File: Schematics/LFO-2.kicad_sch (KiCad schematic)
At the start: 81 parts, among them J16 Conn_01x03, J17 Conn_01x10h, J18 Conn_01x05, J19 Conn_01x03, J89 Conn_01x03, Q12 BSS138, Q13 BSS138, U41 LM324, U42 LM324, U43 ADG419BN, U44 LM78L05, U45 SSI2130, U93 PCF8574, U94 AMS1117-3.3

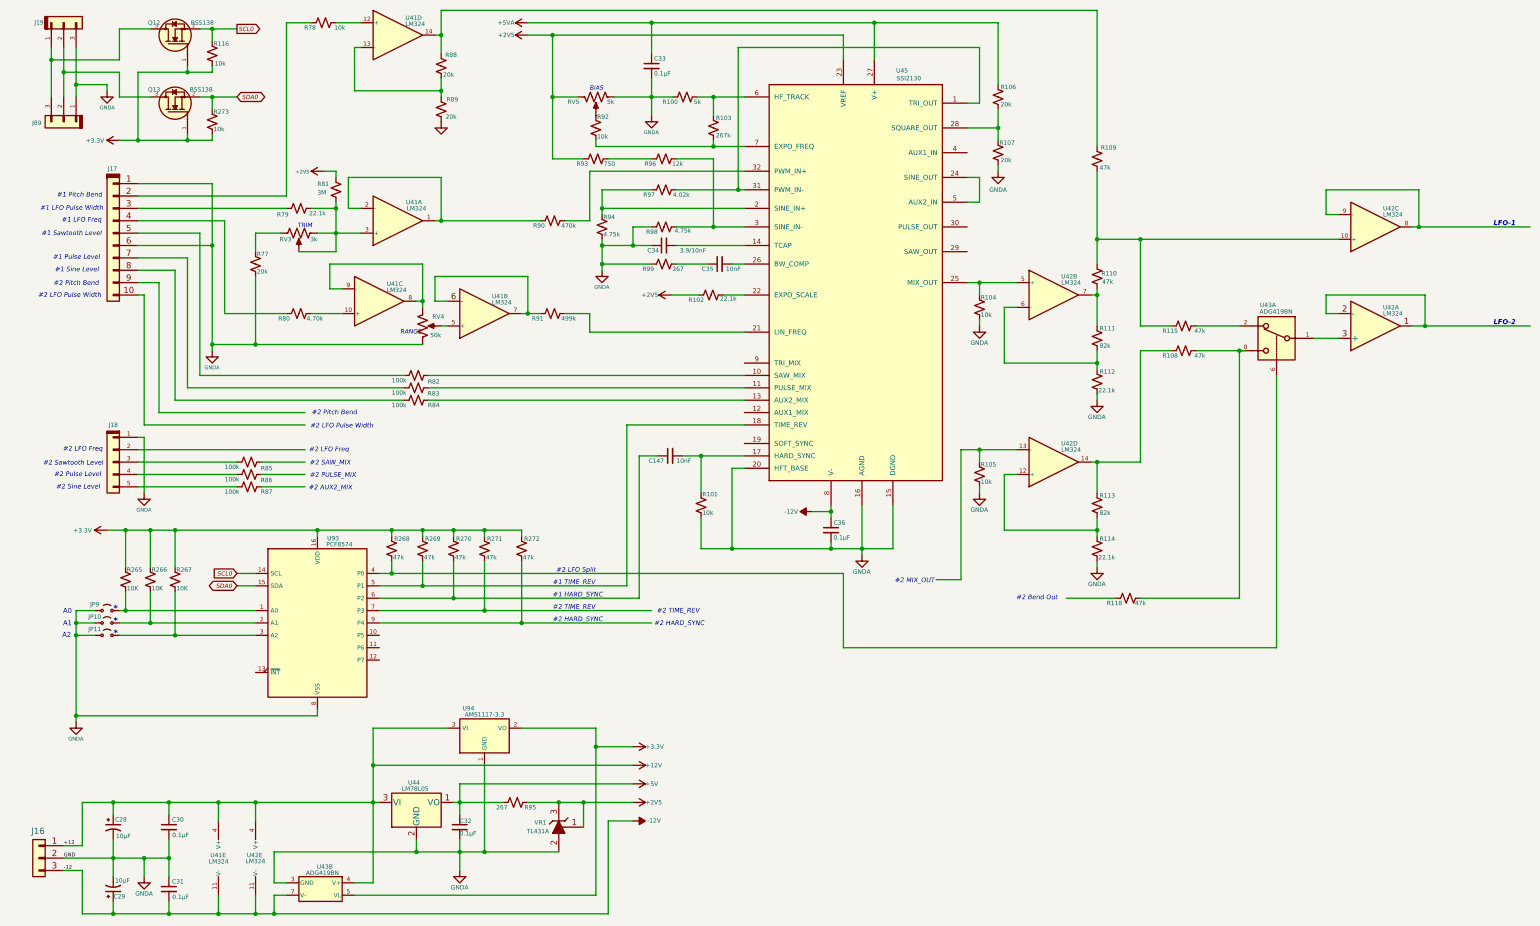
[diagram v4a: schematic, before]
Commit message: Cleaned up page advance on display controls.
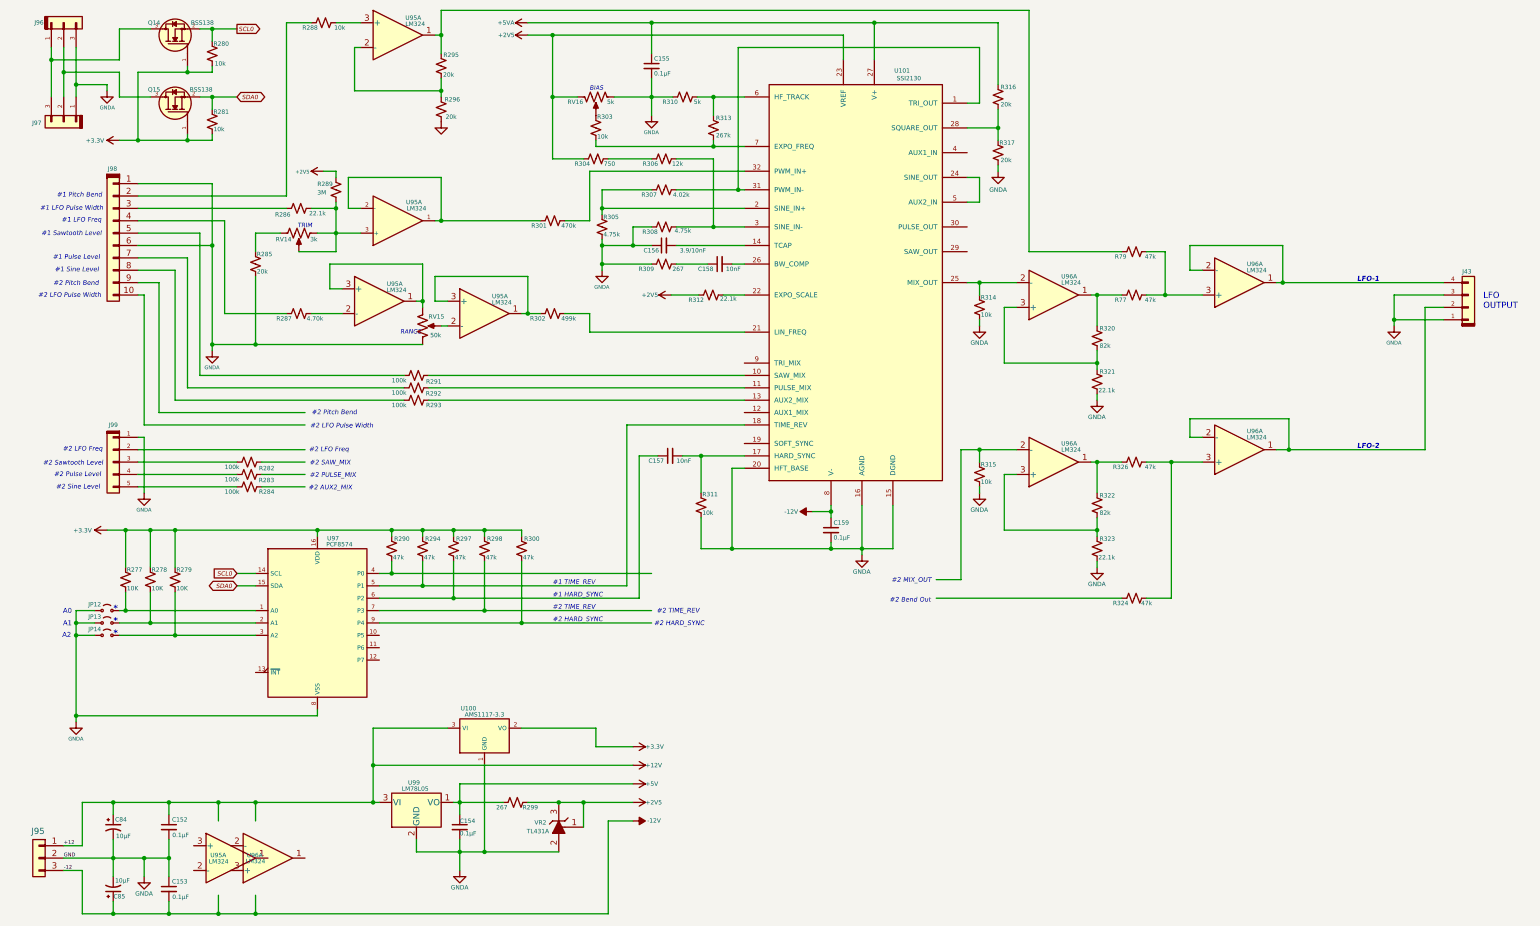
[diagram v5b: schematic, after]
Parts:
- removed R109, R110, R115: 47k, symbol Device:R_Small_US
- removed U43: ADG419BN, Package_DIP:DIP-8_W7.62mm, symbol Analog_Switch:ADG419BN
- added J43: Conn_01x04, symbol My Connectors:Conn_01x04
- added R77, R79: 47k, symbol Device:R_Small_US
- renumbered C30 to C152, C31 to C153, C32 to C154, C33 to C155, C34 to C156, C147 to C157, C35 to C158, C36 to C159, C28 to C84, C29 to C85, J16 to J95, J19 to J96, J89 to J97, J17 to J98, J18 to J99, JP9 to JP12, JP10 to JP13, JP11 to JP14, Q12 to Q14, Q13 to Q15, R265 to R277, R266 to R278, R267 to R279, R116 to R280, R273 to R281, R85 to R282, R86 to R283, R87 to R284, R77 to R285, R79 to R286, R80 to R287, R78 to R288, R81 to R289, R268 to R290, R82 to R291, R83 to R292, R84 to R293, R269 to R294, R88 to R295, R89 to R296, R270 to R297, R271 to R298, R95 to R299, R272 to R300, R90 to R301, R91 to R302, R92 to R303, R93 to R304, R94 to R305, R96 to R306, R97 to R307, R98 to R308, R99 to R309, R100 to R310, R101 to R311, R102 to R312, R103 to R313, R104 to R314, R105 to R315, R106 to R316, R107 to R317, R111 to R320, R112 to R321, R113 to R322, R114 to R323, R118 to R324, R108 to R326, RV3 to RV14, RV4 to RV15, RV5 to RV16, U94 to U100, U45 to U101, U41 to U95, U42 to U96, U93 to U97, U44 to U99, VR1 to VR2
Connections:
- net +12V: no longer U95.4 (V+), U96.4 (V+)
- net -12V: no longer U95.11 (V-), U96.11 (V-)
- net GNDA: now also J43.1 (Pin_1), J43.3 (Pin_3)
- net at R322.2, R323.1: now also U96.3 (+); no longer U96.12 (+)
- net at R315.1: now also U96.2 (-); no longer U96.13 (-)
- net at R322.1, R326.1: now also U96.1; no longer U96.14
- net at R324.2, R326.2: now also U96.3 (+)
- net at R314.1, U101.25 (MIX_OUT): now also U96.2 (-); no longer U96.5 (+)
- net at R320.2, R321.1: now also U96.3 (+); no longer U96.6 (-)
- net at R320.1: now also U96.1, R77.1; no longer U96.7
- net at R288.2: now also U95.3 (+); no longer U95.12 (+)
- net at R295.1, R296.1: now also U95.2 (-); no longer U95.13 (-)
- net at R295.2: now also U95.1, R79.1; no longer U95.14
- net at R287.2: now also U95.2 (-); no longer U95.10 (+)
- net at U96.1, U96.2 (-): now also J43.2 (Pin_2)
- new net: R302.1, U95.1, U95.3 (+)
- new net: RV15. (2), U95.2 (-)
- new net: RV15. (2), U95.1, U95.3 (+)
- new net: J43.4 (Pin_4), U96.1, U96.2 (-)
- new net: R77.2, R79.2, U96.3 (+)
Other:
- note added: "LFO OUTPUT"
- note removed: "#2 LFO Split"
- moved on the sheet: R324, R326, U96A

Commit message: minor adjustments for modulation control interface.
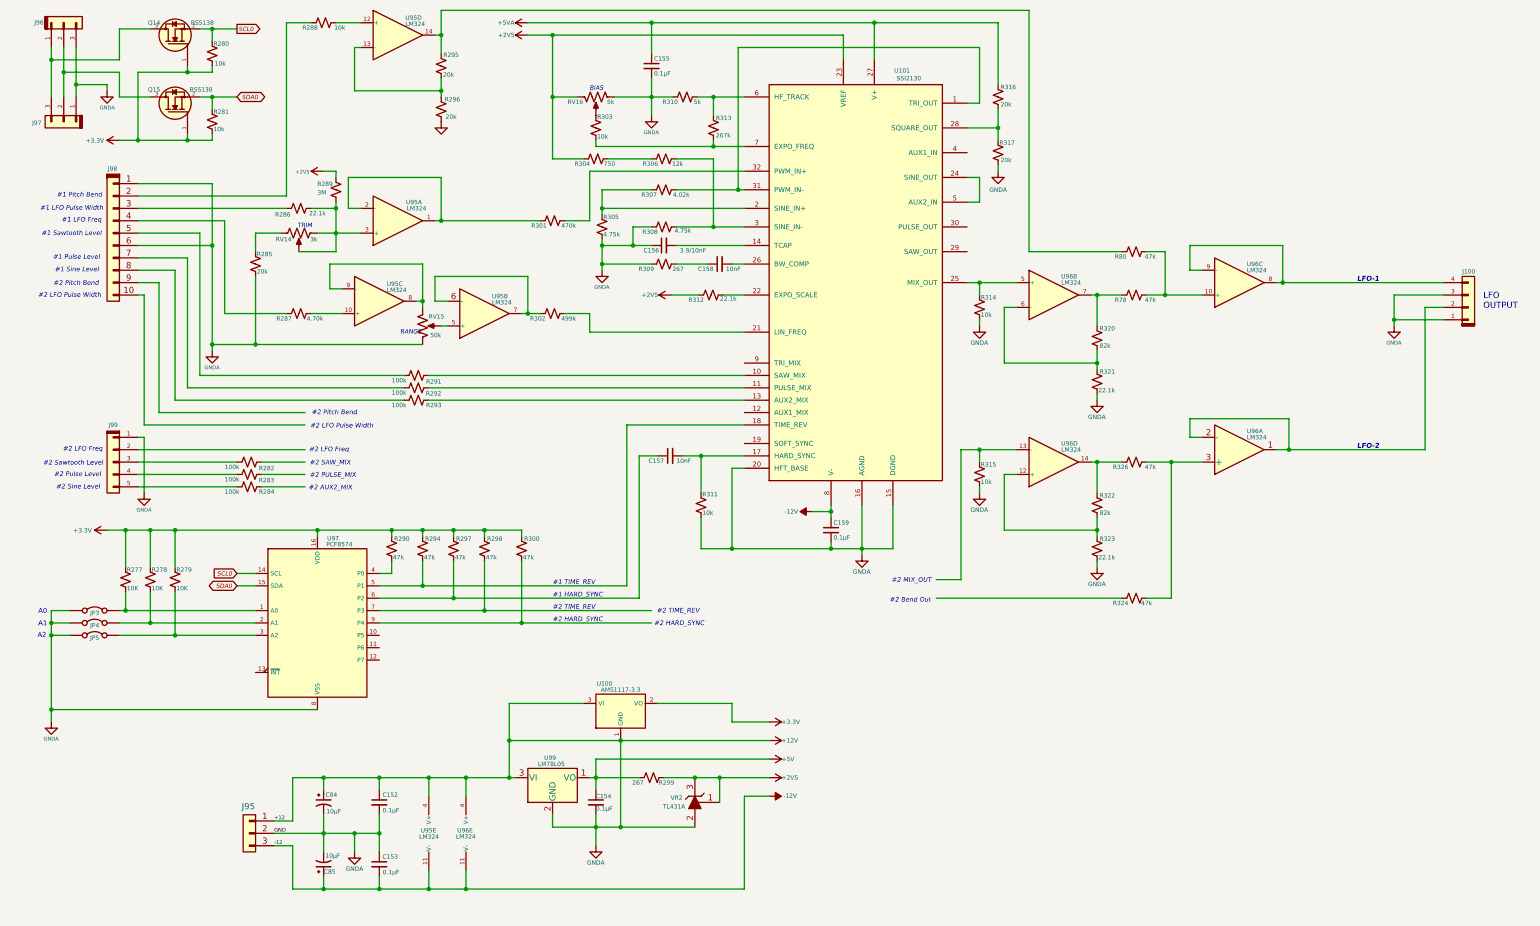
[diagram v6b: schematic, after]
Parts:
- removed JP12, JP13, JP14: Jumper_2_Small_Open, symbol Jumper:Jumper_2_Small_Open
- added JP3, JP4, JP5: Jumper_2_Bridged, symbol Jumper:Jumper_2_Bridged
- renumbered J43 to J100, R77 to R78, R79 to R80
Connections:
- net +12V: now also C152.2, C153.1, C154.2, C155.2, C156.1, C159.2, C84.2, C85.2, J100.1 (Pin_1), J100.3 (Pin_3), J95.2 (Pin_2), J96.3 (Pin_3), J97.1 (Pin_1), J98.1 (Pin_1), J98.6 (Pin_6), J99.1 (Pin_1), R285.2, R296.2, R305.2, R308.1, R309.1, R310.1, R311.2, R314.2, R315.2, R317.2, R321.2, R323.2, RV15. (2), RV16. (2), U100.1 (GND), U101.15 (DGND), U101.16 (AGND), U101.20 (HFT_BASE), U95.4 (V+), U96.4 (V+), U97.8 (VSS), U99.2 (GND), VR2.2 (A), JP3.1 (A), JP4.1 (A), JP5.1 (A)
- net -12V: now also U95.11 (V-), U96.11 (V-)
- net at R322.1, R326.1: now also U96.14; no longer U96.1
- net at R315.1: now also U96.13 (-); no longer U96.2 (-)
- net at R322.2, R323.1: now also U96.12 (+); no longer U96.3 (+)
- net at R320.1, R78.1: now also U96.7; no longer U96.1
- net at R314.1, U101.25 (MIX_OUT): now also U96.5 (+); no longer U96.2 (-)
- net at R320.2, R321.1: now also U96.6 (-); no longer U96.3 (+)
- net at R295.2, R80.1: now also U95.14; no longer U95.1
- net at R295.1, R296.1: now also U95.13 (-); no longer U95.2 (-)
- net at R288.2: now also U95.12 (+); no longer U95.3 (+)
- net at R287.2: now also U95.10 (+); no longer U95.2 (-)
- net at R278.2, U97.2 (A1): now also JP4.2 (B)
- net at R78.2, R80.2: now also U96.10 (+); no longer U96.3 (+)
- net at R279.2, U97.3 (A2): now also JP5.2 (B)
- net at R277.2, U97.1 (A0): now also JP3.2 (B)
- removed net GNDA: C152.2, C153.1, C154.2, C155.2, C156.1, C159.2, C84.2, C85.2, J100.1 (Pin_1), J100.3 (Pin_3), J95.2 (Pin_2), J96.3 (Pin_3), J97.1 (Pin_1), J98.1 (Pin_1), J98.6 (Pin_6), J99.1 (Pin_1), R285.2, R296.2, R305.2, R308.1, R309.1, R310.1, R311.2, R314.2, R315.2, R317.2, R321.2, R323.2, RV15. (2), RV16. (2), U100.1 (GND), U101.15 (DGND), U101.16 (AGND), U101.20 (HFT_BASE), U97.8 (VSS), U99.2 (GND), VR2.2 (A)
- new net: RV15. (2), U95.5 (+)
- new net: R302.1, U95.6 (-), U95.7
- new net: RV15. (2), U95.8, U95.9 (-)
- new net: J100.4 (Pin_4), U96.8, U96.9 (-)
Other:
- note removed: "*"
- moved on the sheet: C152, C153, C154, C84, C85, J95, R299, U100, U99, VR2

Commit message: Added support hardware for LFO output matrix and calibration analog to digital converter.
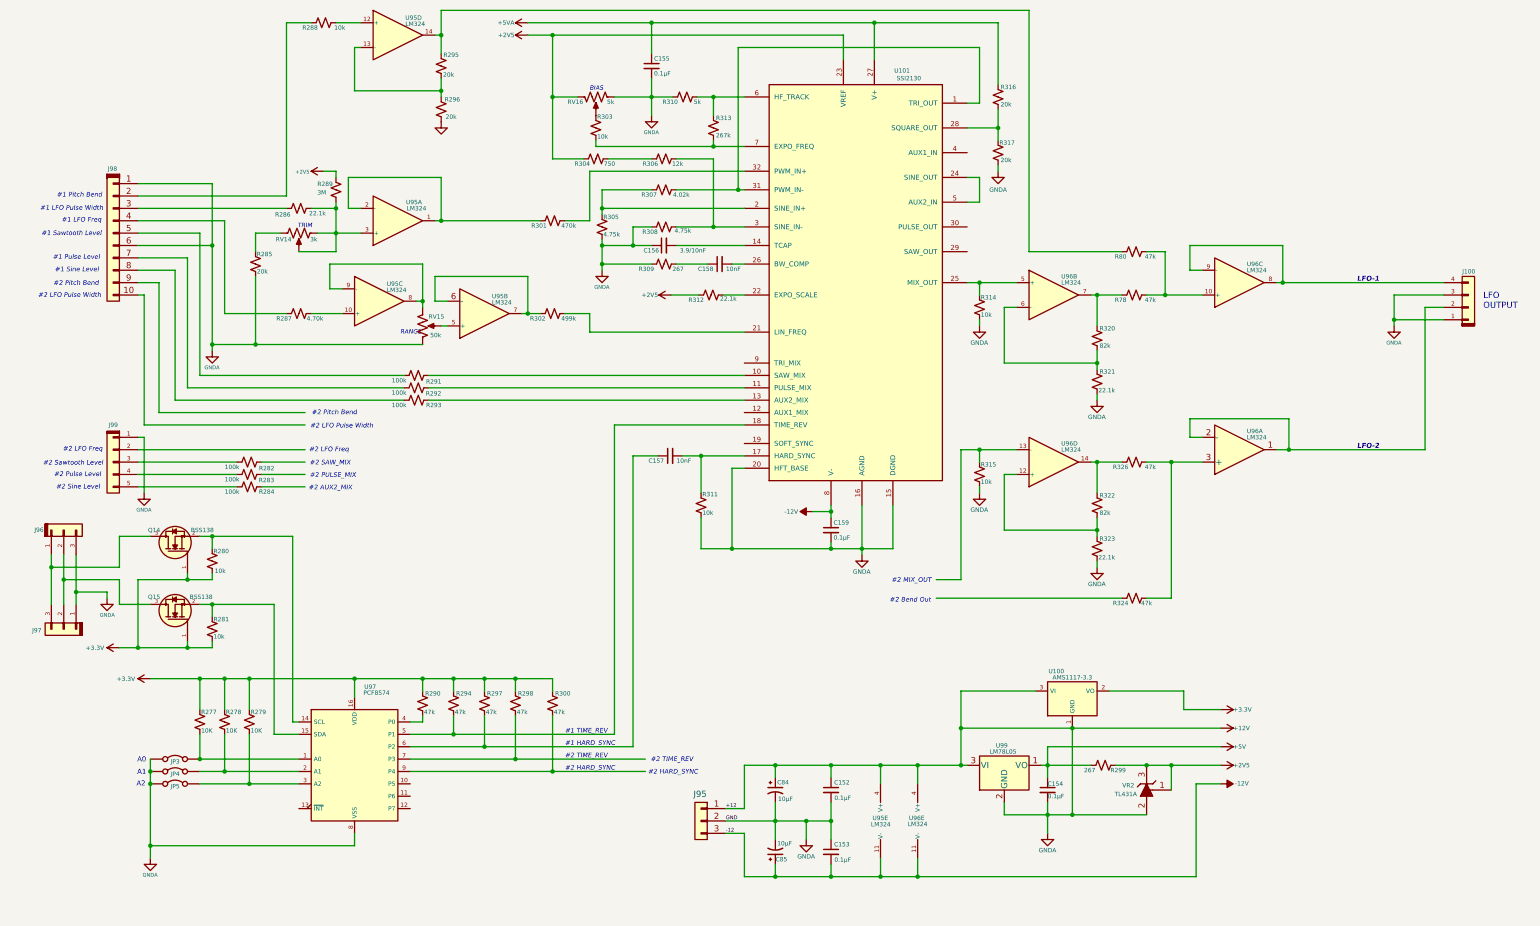
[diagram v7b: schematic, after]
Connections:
- net SCL0: no longer names the net of Q14.2, R280.1, U97.14 (SCL)
- net SDA0: no longer names the net of Q15.2, R281.1, U97.15 (SDA)
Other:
- moved on the sheet: C152, C153, C154, C84, C85, J95, J96, J97, JP3, JP4, JP5, Q14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

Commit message: All Oscillators have thier own D/A converters and both LFOs are working.  Callibration functions.
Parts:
- added R325, R327: 100k, symbol Device:R_Small_US
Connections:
- net +12V: now also R325.2, R327.1
- net at R322.2, R323.1: now also U96.2 (-); no longer U96.12 (+)
- net at U96.13 (-): now also J100.2 (Pin_2), U96.14, R327.2; no longer R315.1
- net at R322.1, R326.1: now also U96.1; no longer U96.14
- net at R324.2, R326.2: now also U96.12 (+); no longer U96.3 (+)
- net at R286.2, R289.2, RV14. (2): now also U95.2 (-); no longer U95.3 (+)
- net at J100.4 (Pin_4), U96.8, U96.9 (-): now also R325.1
- net at R301.1, U95.1: now also U95.3 (+); no longer U95.2 (-)
- new net: R315.1, U96.3 (+)
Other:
- moved on the sheet: R315, R322, R323, R326, U96A, U96D
